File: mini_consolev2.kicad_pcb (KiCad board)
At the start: 2 copper layers, 82.5 x 44.9 mm, 39 parts, among them J1 SWD, J2 Conn_01x20, J3 Conn_01x20, J4 TYPE-C-31-M-12, SW1 SW_Push, SW2 SW_Push, SW3 SW_Push, SW4 SW_Push, U1 STM32G070CBT6, U2 AMS1117-3.3

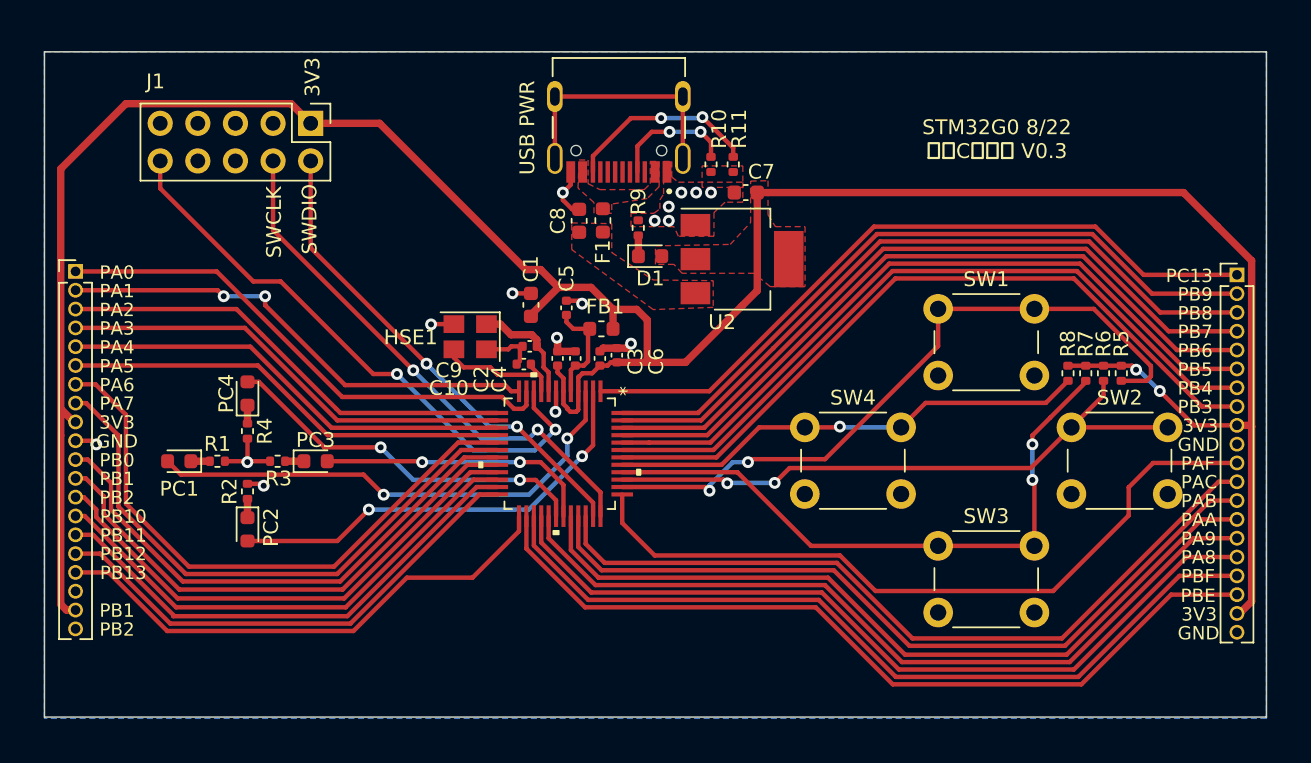
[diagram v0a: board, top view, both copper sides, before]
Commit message: Fixed usbc port
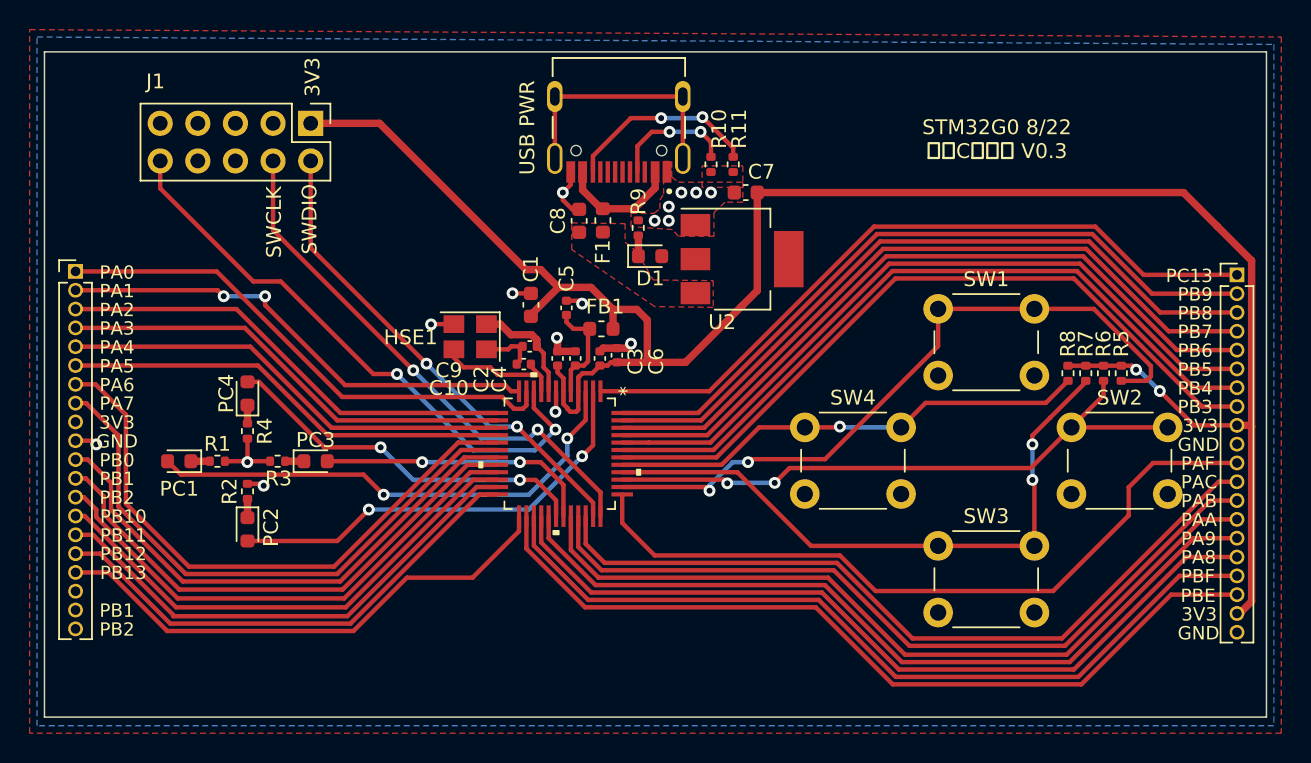
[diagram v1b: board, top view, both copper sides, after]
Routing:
- net +3V3: track 188.9 -> 137.7 mm
- net VBUS: track 0.00 -> 8.30 mm
- removed copper zone on F.Cu, net VBUS
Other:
- board text added: "JLCJLCJLCJLC"
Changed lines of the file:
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@@
     (effects (font (size 0.7 0.7) (thickness 0.15)) (justify mirror))
+  )
+  (gr_text "JLCJLCJLCJLC" (at 200.1 63.1) (layer "B.SilkS")
+    (effects (font (size 1.5 1.5) (thickness 0.3)) (justify mirror))
   )
   (gr_text "STM32G0 8/22\nミニCボード V0.3" (at 190.8 66.4) (layer "F.SilkS")
@@
     (effects (font (size 0.9 0.9) (thickness 0.1)))
   )
-  (segment (start 128.485 85.485) (end 127.6 84.6) (width 0.5) (layer "F.Cu") (net 1))
   (segment (start 167.1375 81.4625) (end 165.1425 81.4625) (width 0.5) (layer "F.Cu") (net 1))
   (segment (start 164 81.68) (end 164.52 81.68) (width 0.3) (layer "F.Cu") (net 1))
@@
   (segment (start 208 97.6) (end 207.185 98.415) (width 0.5) (layer "F.Cu") (net 1))
   (segment (start 199.2 81.69) (end 195.6 81.69) (width 0.3) (layer "F.Cu") (net 1))
-  (segment (start 132 64) (end 143.15 64) (width 0.5) (layer "F.Cu") (net 1))
-  (segment (start 128.6 85.485) (end 128.485 85.485) (width 0.5) (layer "F.Cu") (net 1))
   (segment (start 176.75 73.05) (end 176.75 74.49375) (width 0.5) (layer "F.Cu") (net 1))
   (segment (start 161.8 84.6) (end 161.8 84.539339) (width 0.3) (layer "F.Cu") (net 1))
   (segment (start 163.48 82.2) (end 164 81.68) (width 0.3) (layer "F.Cu") (net 1))
-  (segment (start 127.6 68.4) (end 132 64) (width 0.5) (layer "F.Cu") (net 1))
   (segment (start 208 85.8) (end 208 74.6) (width 0.5) (layer "F.Cu") (net 1))
   (segment (start 167.2 78.6) (end 166.4875 77.8875) (width 0.5) (layer "F.Cu") (net 1))
   (segment (start 174.625 70) (end 174.625 76.61875) (width 0.5) (layer "F.Cu") (net 1))
   (segment (start 161.54 84.279339) (end 161.54 83.4136) (width 0.3) (layer "F.Cu") (net 1))
-  (segment (start 127.6 86.4) (end 127.6 97.8) (width 0.5) (layer "F.Cu") (net 1))
   (segment (start 173.596875 77.646875) (end 169.78125 81.4625) (width 0.5) (layer "F.Cu") (net 1))
   (segment (start 167.1375 81.4625) (end 167.2 81.4) (width 0.5) (layer "F.Cu") (net 1))
   (segment (start 160 75.2) (end 159 75.2) (width 0.5) (layer "F.Cu") (net 1))
-  (segment (start 143.15 64) (end 144.475 65.325) (width 0.5) (layer "F.Cu") (net 1))
-  (segment (start 127.6 86.4) (end 127.6 84.6) (width 0.5) (layer "F.Cu") (net 1))
   (segment (start 167.2 81.4) (end 167.2 78.6) (width 0.5) (layer "F.Cu") (net 1))
   (segment (start 162.625465 82.4) (end 162.825465 82.2) (width 0.3) (layer "F.Cu") (net 1))
@@
   (segment (start 161.2 76.4) (end 160 75.2) (width 0.5) (layer "F.Cu") (net 1))
   (segment (start 162.4 84.8) (end 162 84.8) (width 0.3) (layer "F.Cu") (net 1))
-  (segment (start 127.985 98.185) (end 128.6 98.185) (width 0.5) (layer "F.Cu") (net 1))
   (segment (start 207.915 85.715) (end 208 85.8) (width 0.5) (layer "F.Cu") (net 1))
   (segment (start 201.8 83.4) (end 204.115 85.715) (width 0.3) (layer "F.Cu") (net 1))
@@
   (segment (start 162.54 83.4136) (end 162.54 84.66) (width 0.3) (layer "F.Cu") (net 1))
   (segment (start 161.54 83.4136) (end 161.54 82.54) (width 0.3) (layer "F.Cu") (net 1))
-  (segment (start 127.6 97.8) (end 127.985 98.185) (width 0.5) (layer "F.Cu") (net 1))
   (segment (start 159.3425 78.2575) (end 161.2 76.4) (width 0.5) (layer "F.Cu") (net 1))
   (segment (start 164.8875 77.8875) (end 163.4 76.4) (width 0.5) (layer "F.Cu") (net 1))
   (segment (start 208 74.6) (end 205.675 72.275) (width 0.5) (layer "F.Cu") (net 1))
   (segment (start 162 84.8) (end 161.8 84.6) (width 0.3) (layer "F.Cu") (net 1))
-  (segment (start 127.6 84.6) (end 127.6 68.4) (width 0.5) (layer "F.Cu") (net 1))
   (segment (start 199.2 81.69) (end 199.9295 81.69) (width 0.3) (layer "F.Cu") (net 1))
   (segment (start 199.9295 81.69) (end 200.2 81.9605) (width 0.3) (layer "F.Cu") (net 1))
@@
   (segment (start 167.5 65.9) (end 168.7 65.9) (width 0.3) (layer "F.Cu") (net 10))
   (segment (start 171.5 67.59) (end 171.5 66.6) (width 0.3) (layer "F.Cu") (net 10))
+  (segment (start 166.53 66.87) (end 167.5 65.9) (width 0.3) (layer "F.Cu") (net 10))
   (segment (start 171.5 66.6) (end 170.8 65.9) (width 0.3) (layer "F.Cu") (net 10))
-  (segment (start 166.53 66.87) (end 167.5 65.9) (width 0.3) (layer "F.Cu") (net 10))
   (via (at 170.8 65.9) (size 0.8) (drill 0.4) (layers "F.Cu" "B.Cu") (net 10))
   (via (at 168.7 65.9) (size 0.8) (drill 0.4) (layers "F.Cu" "B.Cu") (net 10))
-  (segment (start 170.7 65.8) (end 170.8 65.9) (width 0.2) (layer "B.Cu") (net 10))
-  (segment (start 168.7 65.9) (end 170.8 65.9) (width 0.3) (layer "B.Cu") (net 10))
-  (segment (start 168.8 65.9) (end 168.7 65.8) (width 0.2) (layer "B.Cu") (net 10))
+  (segment (start 170.8 65.9) (end 168.7 65.9) (width 0.3) (layer "B.Cu") (net 10))
   (segment (start 146.277 93.523) (end 140.208 93.523) (width 0.3) (layer "F.Cu") (net 11))
   (segment (start 163.540001 83.4136) (end 163.540001 87.059999) (width 0.3) (layer "F.Cu") (net 11))
@@
   (segment (start 158.6 89.4) (end 151.4 89.4) (width 0.3) (layer "B.Cu") (net 15))
   (segment (start 140.208 91.948) (end 140.208 90.682) (width 0.5) (layer "F.Cu") (net 16))
+  (segment (start 166.3225 71.09375) (end 164.2 71.09375) (width 0.5) (layer "F.Cu") (net 17))
+  (segment (start 162.83 69.83) (end 164.09375 71.09375) (width 0.5) (layer "F.Cu") (net 17))
+  (segment (start 164.09375 71.09375) (end 164.2 71.09375) (width 0.5) (layer "F.Cu") (net 17))
+  (segment (start 167.73 68.61125) (end 167.73 69.68625) (width 0.5) (layer "F.Cu") (net 17))
+  (segment (start 162.83 68.61125) (end 162.83 69.83) (width 0.5) (layer "F.Cu") (net 17))
+  (segment (start 167.73 69.68625) (end 166.3225 71.09375) (width 0.5) (layer "F.Cu") (net 17))
   (segment (start 163.540001 90.9359) (end 158.404101 85.8) (width 0.3) (layer "F.Cu") (net 18))
   (segment (start 163.540001 91.8464) (end 163.540001 90.9359) (width 0.3) (layer "F.Cu") (net 18))
@@
   (segment (start 180.252 85.852) (end 184.334 85.852) (width 0.3) (layer "B.Cu") (net 68))
   (segment (start 180.2 85.8) (end 180.252 85.852) (width 0.3) (layer "B.Cu") (net 68))
-  (zone (net 1) (net_name "+3V3") (layer "F.Cu") (hatch edge 0.508)
-    (connect_pads yes (clearance 0.3))
-    (min_thickness 0.25) (filled_areas_thickness no)
-    (fill yes (thermal_gap 0.508) (thermal_bridge_width 0.508))
-    (polygon
-      (pts
-        (xy 175.35 71.5)
-        (xy 175.85 72.3)
-        (xy 177.85 72.3)
-        (xy 177.85 76.35)
-        (xy 175.5 76.35)
-        (xy 174.4 75.45)
-        (xy 169.55 75.45)
-        (xy 169 74.85)
-        (xy 167.75 74.85)
-        (xy 167.75 73.6)
-        (xy 172.8 73.5)
-        (xy 174.175 72.025)
-        (xy 174.175 69.225)
-        (xy 175.35 69.2)
-      )
-    )
-  )
   (zone (net 2) (net_name "GND") (layer "F.Cu") (hatch edge 0.508)
+    (priority 2)
     (connect_pads yes (clearance 0.3))
     (min_thickness 0.254) (filled_areas_thickness no)
@@
     )
   )
+  (zone (net 1) (net_name "+3V3") (layer "F.Cu") (hatch edge 0.508)
+    (connect_pads (clearance 0.3))
+    (min_thickness 0.254) (filled_areas_thickness no)
+    (fill yes (thermal_gap 0.508) (thermal_bridge_width 0.508))
+    (polygon
+      (pts
+        (xy 210 59.5)
+        (xy 210 106.5)
+        (xy 125.5 106.5)
+        (xy 125.5 59)
+      )
+    )
+  )
   (zone (net 4) (net_name "Net-(C8-Pad1)") (layer "F.Cu") (hatch edge 0.508)
+    (priority 2)
     (connect_pads yes (clearance 0.3))
     (min_thickness 0.25) (filled_areas_thickness no)
@@
     (polygon
       (pts
-        (xy 164.8 72.1)
-        (xy 164.8 73.35)
-        (xy 164.8 74.05)
+        (xy 165.7 72.1)
+        (xy 165.7 73.35)
+        (xy 166.5 74)
         (xy 167.6 75.9)
         (xy 171.65 75.95)
         (xy 171.65 77.75)
-        (xy 167.6 77.9)
+        (xy 167.7 77.7)
         (xy 162.1 73.85)
         (xy 162.1 73.2)
@@
   )
   (zone (net 2) (net_name "GND") (layer "F.Cu") (hatch edge 0.508)
-    (connect_pads yes (clearance 0.3))
+    (priority 2)
+    (connect_pads (clearance 0.3))
     (min_thickness 0.25) (filled_areas_thickness no)
     (fill yes (thermal_gap 0.508) (thermal_bridge_width 0.508))
@@
         (xy 171.7 72.95)
         (xy 169.3 72.95)
-        (xy 169 72.3)
+        (xy 168.9 72.5)
         (xy 166.1 72.3)
         (xy 166.1 71.4)
@@
     )
   )
-  (zone (net 17) (net_name "VBUS") (layer "F.Cu") (hatch edge 0.508)
-    (connect_pads yes (clearance 0.3))
-    (min_thickness 0.25) (filled_areas_thickness no)
-    (fill yes (thermal_gap 0.508) (thermal_bridge_width 0.508))
-    (polygon
-      (pts
-        (xy 163.2 69.4)
-        (xy 164 69.8)
-        (xy 167 69.8)
-        (xy 167.4 69.4)
-        (xy 167.4 67.9)
-        (xy 168 67.9)
-        (xy 168 69.6)
-        (xy 167.2 70.4)
-        (xy 164.8 70.775)
-        (xy 164.8 71.4)
-        (xy 163.6 71.4)
-        (xy 163.6 70.675)
-        (xy 162.521952 69.697562)
-        (xy 162.6 67.8)
-        (xy 163.2 67.8)
-      )
-    )
-  )
   (zone (net 2) (net_name "GND") (layer "B.Cu") (hatch edge 0.508)
     (connect_pads (clearance 0.508))
@@
     (polygon
       (pts
-        (xy 209 105.5)
-        (xy 126.5 105.5)
-        (xy 126.5 60.5)
-        (xy 209 60.5)
+        (xy 209.5 106)
+        (xy 126 106)
+        (xy 126 59.5)
+        (xy 209.5 60)
       )
     )
